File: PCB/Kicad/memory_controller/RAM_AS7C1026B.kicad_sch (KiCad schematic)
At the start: 2 parts, among them U25 AS7C1026B-10TCN

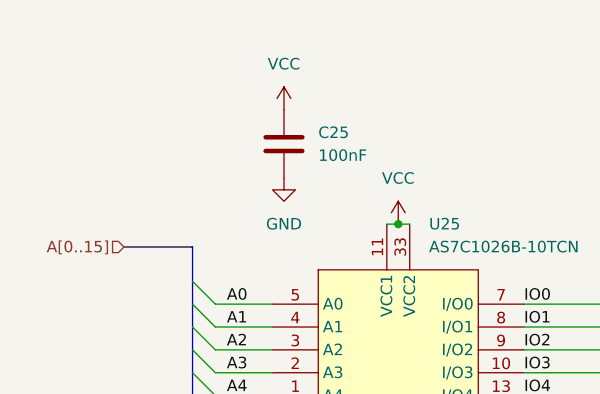
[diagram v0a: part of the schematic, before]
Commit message: decoupling C RAM ROM
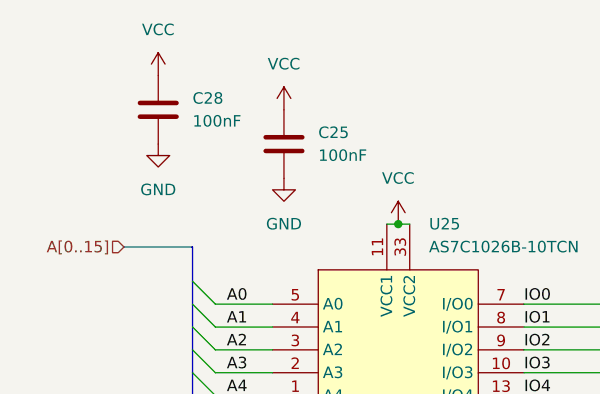
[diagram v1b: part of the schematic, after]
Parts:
- added C28: 100nF, Capacitor_SMD:C_0402_1005Metric, symbol Device:C
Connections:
- net GND: now also C28.1
- net VCC: now also C28.2
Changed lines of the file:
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@@
+	)
+	(symbol
+		(lib_id "Device:C")
+		(at 123.19 45.72 180)
+		(unit 1)
+		(body_style 1)
+		(exclude_from_sim no)
+		(in_bom yes)
+		(on_board yes)
+		(in_pos_files yes)
+		(dnp no)
+		(fields_autoplaced yes)
+		(property "Reference" "C28"
+			(at 127 44.4499 0)
+			(show_name no)
+			(do_not_autoplace no)
+			(effects
+				(font
+					(size 1.27 1.27)
+				)
+				(justify right)
+			)
+		)
+		(property "Value" "100nF"
+			(at 127 46.9899 0)
+			(show_name no)
+			(do_not_autoplace no)
+			(effects
+				(font
+					(size 1.27 1.27)
+				)
+				(justify right)
+			)
+		)
+		(property "Footprint" "Capacitor_SMD:C_0402_1005Metric"
+			(at 122.2248 41.91 0)
+			(hide yes)
+			(show_name no)
+			(do_not_autoplace no)
+			(effects
+				(font
+					(size 1.27 1.27)
+				)
+			)
+		)
+		(property "Datasheet" "https://www.tme.eu/pl/details/cs1005x7r104k100nr/kondensatory-mlcc-smd/samwha/"
+			(at 123.19 45.72 0)
+			(hide yes)
+			(show_name no)
+			(do_not_autoplace no)
+			(effects
+				(font
+					(size 1.27 1.27)
+				)
+			)
+		)
+		(property "Description" "Unpolarized capacitor"
+			(at 123.19 45.72 0)
+			(hide yes)
+			(show_name no)
+			(do_not_autoplace no)
+			(effects
+				(font
+					(size 1.27 1.27)
+				)
+			)
+		)
+		(pin "2"
+		)
+		(pin "1"
+		)
+		(instances
+			(project "memory_controller"
+				(path "/dccec861-b967-466c-843e-d6d1ad6064ce/65198342-3b70-4e1d-8493-7cbe3d0407e3"
+					(reference "C28")
+					(unit 1)
+				)
+			)
+		)
 	)
 	(symbol
@@
 	(symbol
 		(lib_id "power:VCC")
+		(at 123.19 41.91 0)
+		(unit 1)
+		(body_style 1)
+		(exclude_from_sim no)
+		(in_bom yes)
+		(on_board yes)
+		(in_pos_files yes)
+		(dnp no)
+		(fields_autoplaced yes)
+		(property "Reference" "#PWR0188"
+			(at 123.19 45.72 0)
+			(hide yes)
+			(show_name no)
+			(do_not_autoplace no)
+			(effects
+				(font
+					(size 1.27 1.27)
+				)
+			)
+		)
+		(property "Value" "VCC"
+			(at 123.19 36.83 0)
+			(show_name no)
+			(do_not_autoplace no)
+			(effects
+				(font
+					(size 1.27 1.27)
+				)
+			)
+		)
+		(property "Footprint" ""
+			(at 123.19 41.91 0)
+			(hide yes)
+			(show_name no)
+			(do_not_autoplace no)
+			(effects
+				(font
+					(size 1.27 1.27)
+				)
+			)
+		)
+		(property "Datasheet" ""
+			(at 123.19 41.91 0)
+			(hide yes)
+			(show_name no)
+			(do_not_autoplace no)
+			(effects
+				(font
+					(size 1.27 1.27)
+				)
+			)
+		)
+		(property "Description" "Power symbol creates a global label with name \"VCC\""
+			(at 123.19 41.91 0)
+			(hide yes)
+			(show_name no)
+			(do_not_autoplace no)
+			(effects
+				(font
+					(size 1.27 1.27)
+				)
+			)
+		)
+		(pin "1"
+		)
+		(instances
+			(project "memory_controller"
+				(path "/dccec861-b967-466c-843e-d6d1ad6064ce/65198342-3b70-4e1d-8493-7cbe3d0407e3"
+					(reference "#PWR0188")
+					(unit 1)
+				)
+			)
+		)
+	)
+	(symbol
+		(lib_id "power:VCC")
 		(at 149.86 58.42 0)
 		(unit 1)
@@
 					(unit 1)
 				)
+			)
+		)
+	)
+	(symbol
+		(lib_id "power:GND")
+		(at 123.19 49.53 0)
+		(unit 1)
+		(body_style 1)
+		(exclude_from_sim no)
+		(in_bom yes)
+		(on_board yes)
+		(in_pos_files yes)
+		(dnp no)
+		(fields_autoplaced yes)
+		(property "Reference" "#PWR0189"
+			(at 123.19 55.88 0)
+			(hide yes)
+			(show_name no)
+			(do_not_autoplace no)
+			(effects
+				(font
+					(size 1.27 1.27)
+				)
+			)
+		)
+		(property "Value" "GND"
+			(at 123.19 54.61 0)
+			(show_name no)
+			(do_not_autoplace no)
+			(effects
+				(font
+					(size 1.27 1.27)
+				)
+			)
+		)
+		(property "Footprint" ""
+			(at 123.19 49.53 0)
+			(hide yes)
+			(show_name no)
+			(do_not_autoplace no)
+			(effects
+				(font
+					(size 1.27 1.27)
+				)
+			)
+		)
+		(property "Datasheet" ""
+			(at 123.19 49.53 0)
+			(hide yes)
+			(show_name no)
+			(do_not_autoplace no)
+			(effects
+				(font
+					(size 1.27 1.27)
+				)
+			)
+		)
+		(property "Description" "Power symbol creates a global label with name \"GND\" , ground"
+			(at 123.19 49.53 0)
+			(hide yes)
+			(show_name no)
+			(do_not_autoplace no)
+			(effects
+				(font
+					(size 1.27 1.27)
+				)
+			)
+		)
+		(pin "1"
+		)
+		(instances
+			(project "memory_controller"
+				(path "/dccec861-b967-466c-843e-d6d1ad6064ce/65198342-3b70-4e1d-8493-7cbe3d0407e3"
+					(reference "#PWR0189")
+					(unit 1)
+				)

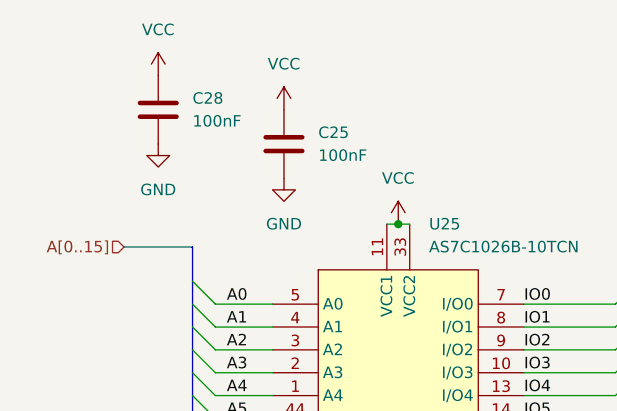
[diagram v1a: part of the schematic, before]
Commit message: board size + ground vias
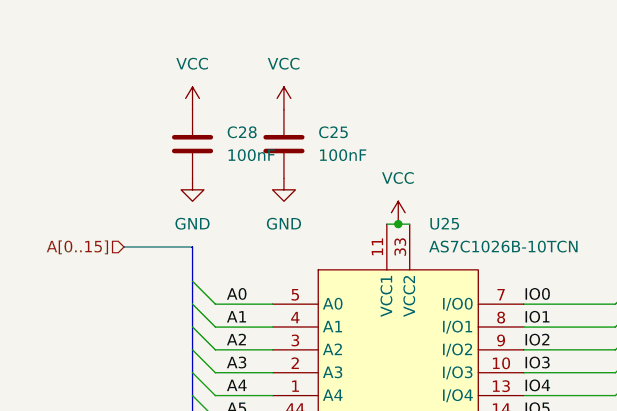
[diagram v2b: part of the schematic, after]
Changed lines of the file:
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@@
-	)
-	(symbol
-		(lib_id "Device:C")
-		(at 123.19 45.72 180)
-		(unit 1)
-		(body_style 1)
-		(exclude_from_sim no)
-		(in_bom yes)
-		(on_board yes)
-		(in_pos_files yes)
-		(dnp no)
-		(fields_autoplaced yes)
-		(property "Reference" "C28"
-			(at 127 44.4499 0)
-			(show_name no)
-			(do_not_autoplace no)
-			(effects
-				(font
-					(size 1.27 1.27)
-				)
-				(justify right)
-			)
-		)
-		(property "Value" "100nF"
-			(at 127 46.9899 0)
-			(show_name no)
-			(do_not_autoplace no)
-			(effects
-				(font
-					(size 1.27 1.27)
-				)
-				(justify right)
-			)
-		)
-		(property "Footprint" "Capacitor_SMD:C_0402_1005Metric"
-			(at 122.2248 41.91 0)
-			(hide yes)
-			(show_name no)
-			(do_not_autoplace no)
-			(effects
-				(font
-					(size 1.27 1.27)
-				)
-			)
-		)
-		(property "Datasheet" "https://www.tme.eu/pl/details/cs1005x7r104k100nr/kondensatory-mlcc-smd/samwha/"
-			(at 123.19 45.72 0)
-			(hide yes)
-			(show_name no)
-			(do_not_autoplace no)
-			(effects
-				(font
-					(size 1.27 1.27)
-				)
-			)
-		)
-		(property "Description" "Unpolarized capacitor"
-			(at 123.19 45.72 0)
-			(hide yes)
-			(show_name no)
-			(do_not_autoplace no)
-			(effects
-				(font
-					(size 1.27 1.27)
-				)
-			)
-		)
-		(pin "2"
-		)
-		(pin "1"
-		)
-		(instances
-			(project "memory_controller"
-				(path "/dccec861-b967-466c-843e-d6d1ad6064ce/65198342-3b70-4e1d-8493-7cbe3d0407e3"
-					(reference "C28")
-					(unit 1)
-				)
-			)
-		)
 	)
 	(symbol
@@
 	)
 	(symbol
-		(lib_id "power:VCC")
-		(at 123.19 41.91 0)
+		(lib_id "Device:C")
+		(at 127 49.53 180)
 		(unit 1)
 		(body_style 1)
@@
 		(dnp no)
 		(fields_autoplaced yes)
-		(property "Reference" "#PWR0188"
-			(at 123.19 45.72 0)
-			(hide yes)
-			(show_name no)
-			(do_not_autoplace no)
-			(effects
-				(font
-					(size 1.27 1.27)
-				)
-			)
-		)
-		(property "Value" "VCC"
-			(at 123.19 36.83 0)
-			(show_name no)
-			(do_not_autoplace no)
-			(effects
-				(font
-					(size 1.27 1.27)
-				)
-			)
-		)
-		(property "Footprint" ""
-			(at 123.19 41.91 0)
-			(hide yes)
-			(show_name no)
-			(do_not_autoplace no)
-			(effects
-				(font
-					(size 1.27 1.27)
-				)
-			)
-		)
-		(property "Datasheet" ""
-			(at 123.19 41.91 0)
-			(hide yes)
-			(show_name no)
-			(do_not_autoplace no)
-			(effects
-				(font
-					(size 1.27 1.27)
-				)
-			)
-		)
-		(property "Description" "Power symbol creates a global label with name \"VCC\""
-			(at 123.19 41.91 0)
-			(hide yes)
-			(show_name no)
-			(do_not_autoplace no)
-			(effects
-				(font
-					(size 1.27 1.27)
-				)
-			)
+		(property "Reference" "C28"
+			(at 130.81 48.2599 0)
+			(show_name no)
+			(do_not_autoplace no)
+			(effects
+				(font
+					(size 1.27 1.27)
+				)
+				(justify right)
+			)
+		)
+		(property "Value" "100nF"
+			(at 130.81 50.7999 0)
+			(show_name no)
+			(do_not_autoplace no)
+			(effects
+				(font
+					(size 1.27 1.27)
+				)
+				(justify right)
+			)
+		)
+		(property "Footprint" "Capacitor_SMD:C_0402_1005Metric"
+			(at 126.0348 45.72 0)
+			(hide yes)
+			(show_name no)
+			(do_not_autoplace no)
+			(effects
+				(font
+					(size 1.27 1.27)
+				)
+			)
+		)
+		(property "Datasheet" "https://www.tme.eu/pl/details/cs1005x7r104k100nr/kondensatory-mlcc-smd/samwha/"
+			(at 127 49.53 0)
+			(hide yes)
+			(show_name no)
+			(do_not_autoplace no)
+			(effects
+				(font
+					(size 1.27 1.27)
+				)
+			)
+		)
+		(property "Description" "Unpolarized capacitor"
+			(at 127 49.53 0)
+			(hide yes)
+			(show_name no)
+			(do_not_autoplace no)
+			(effects
+				(font
+					(size 1.27 1.27)
+				)
+			)
+		)
+		(pin "2"
 		)
 		(pin "1"
@@
 			(project "memory_controller"
 				(path "/dccec861-b967-466c-843e-d6d1ad6064ce/65198342-3b70-4e1d-8493-7cbe3d0407e3"
-					(reference "#PWR0188")
+					(reference "C28")
 					(unit 1)
 				)
@@
 	)
 	(symbol
-		(lib_id "power:GND")
-		(at 123.19 49.53 0)
-		(unit 1)
-		(body_style 1)
-		(exclude_from_sim no)
-		(in_bom yes)
-		(on_board yes)
-		(in_pos_files yes)
-		(dnp no)
-		(fields_autoplaced yes)
-		(property "Reference" "#PWR0189"
-			(at 123.19 55.88 0)
-			(hide yes)
-			(show_name no)
-			(do_not_autoplace no)
-			(effects
-				(font
-					(size 1.27 1.27)
-				)
-			)
-		)
-		(property "Value" "GND"
-			(at 123.19 54.61 0)
-			(show_name no)
-			(do_not_autoplace no)
-			(effects
-				(font
-					(size 1.27 1.27)
-				)
-			)
-		)
-		(property "Footprint" ""
-			(at 123.19 49.53 0)
-			(hide yes)
-			(show_name no)
-			(do_not_autoplace no)
-			(effects
-				(font
-					(size 1.27 1.27)
-				)
-			)
-		)
-		(property "Datasheet" ""
-			(at 123.19 49.53 0)
-			(hide yes)
-			(show_name no)
-			(do_not_autoplace no)
-			(effects
-				(font
-					(size 1.27 1.27)
-				)
-			)
-		)
-		(property "Description" "Power symbol creates a global label with name \"GND\" , ground"
-			(at 123.19 49.53 0)
-			(hide yes)
-			(show_name no)
-			(do_not_autoplace no)
-			(effects
-				(font
-					(size 1.27 1.27)
-				)
-			)
-		)
-		(pin "1"
-		)
-		(instances
-			(project "memory_controller"
-				(path "/dccec861-b967-466c-843e-d6d1ad6064ce/65198342-3b70-4e1d-8493-7cbe3d0407e3"
-					(reference "#PWR0189")
-					(unit 1)
-				)
-			)
-		)
-	)
-	(symbol
 		(lib_id "power:VCC")
 		(at 137.16 45.72 0)
@@
 				(path "/dccec861-b967-466c-843e-d6d1ad6064ce/65198342-3b70-4e1d-8493-7cbe3d0407e3"
 					(reference "#PWR0168")
+					(unit 1)
+				)
+			)
+		)
+	)
+	(symbol
+		(lib_id "power:VCC")
+		(at 127 45.72 0)
+		(unit 1)
+		(body_style 1)
+		(exclude_from_sim no)
+		(in_bom yes)
+		(on_board yes)
+		(in_pos_files yes)
+		(dnp no)
+		(fields_autoplaced yes)
+		(property "Reference" "#PWR0188"
+			(at 127 49.53 0)
+			(hide yes)
+			(show_name no)
+			(do_not_autoplace no)
+			(effects
+				(font
+					(size 1.27 1.27)
+				)
+			)
+		)
+		(property "Value" "VCC"
+			(at 127 40.64 0)
+			(show_name no)
+			(do_not_autoplace no)
+			(effects
+				(font
+					(size 1.27 1.27)
+				)
+			)
+		)
+		(property "Footprint" ""
+			(at 127 45.72 0)
+			(hide yes)
+			(show_name no)
+			(do_not_autoplace no)
+			(effects
+				(font
+					(size 1.27 1.27)
+				)
+			)
+		)
+		(property "Datasheet" ""
+			(at 127 45.72 0)
+			(hide yes)
+			(show_name no)
+			(do_not_autoplace no)
+			(effects
+				(font
+					(size 1.27 1.27)
+				)
+			)
+		)
+		(property "Description" "Power symbol creates a global label with name \"VCC\""
+			(at 127 45.72 0)
+			(hide yes)
+			(show_name no)
+			(do_not_autoplace no)
+			(effects
+				(font
+					(size 1.27 1.27)
+				)
+			)
+		)
+		(pin "1"
+		)
+		(instances
+			(project "memory_controller"
+				(path "/dccec861-b967-466c-843e-d6d1ad6064ce/65198342-3b70-4e1d-8493-7cbe3d0407e3"
+					(reference "#PWR0188")
 					(unit 1)
 				)
@@
 					(unit 1)
 				)
+			)
+		)
+	)
+	(symbol
+		(lib_id "power:GND")
+		(at 127 53.34 0)
+		(unit 1)
+		(body_style 1)
+		(exclude_from_sim no)
+		(in_bom yes)
+		(on_board yes)
+		(in_pos_files yes)
+		(dnp no)
+		(fields_autoplaced yes)
+		(property "Reference" "#PWR0189"
+			(at 127 59.69 0)
+			(hide yes)
+			(show_name no)
+			(do_not_autoplace no)
+			(effects
+				(font
+					(size 1.27 1.27)
+				)
+			)
+		)
+		(property "Value" "GND"
+			(at 127 58.42 0)
+			(show_name no)
+			(do_not_autoplace no)
+			(effects
+				(font
+					(size 1.27 1.27)
+				)
+			)
+		)
+		(property "Footprint" ""
+			(at 127 53.34 0)
+			(hide yes)
+			(show_name no)
+			(do_not_autoplace no)
+			(effects
+				(font
+					(size 1.27 1.27)
+				)
+			)
+		)
+		(property "Datasheet" ""
+			(at 127 53.34 0)
+			(hide yes)
+			(show_name no)
+			(do_not_autoplace no)
+			(effects
+				(font
+					(size 1.27 1.27)
+				)
+			)
+		)
+		(property "Description" "Power symbol creates a global label with name \"GND\" , ground"
+			(at 127 53.34 0)
+			(hide yes)
+			(show_name no)
+			(do_not_autoplace no)
+			(effects
+				(font
+					(size 1.27 1.27)
+				)
+			)
+		)
+		(pin "1"
+		)
+		(instances
+			(project "memory_controller"
+				(path "/dccec861-b967-466c-843e-d6d1ad6064ce/65198342-3b70-4e1d-8493-7cbe3d0407e3"
+					(reference "#PWR0189")
+					(unit 1)
+				)
